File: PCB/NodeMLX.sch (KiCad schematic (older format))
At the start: 19 parts, among them J1 DS3231, J2 PIR, M1 MICROSD, U1 NodeMCUv2, U2 MLX90621

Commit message: Fixed PCB. Added html generators for live map
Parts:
- removed LED1: RED, 1206, symbol LEDSMT1206-RESCUE-NodeMLX
- added D2: RED, LEDs:LED_1206, symbol LED_ALT
- R8: value 130R -> 330R
- S1: footprint TACTILE-SWITCH-SMD -> toolbox:TACTILE-SWITCH-SMD
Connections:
- net 3.3V: now also R7.1; no longer S1.1, S1.2
- net BUTTON: now also R7.2, S1.1, S1.2, U1.D4 (D4/BOOT(h)); no longer R7.1, S1.3, S1.4, U1.D0
- net GND: now also S1.3, S1.4, D2.1 (K); no longer R7.2
- net LED: now also U1.D0; no longer U1.D1
- net PIR: now also U1.D1; no longer U1.D4 (D4/BOOT(h))
- net at R8.2: now also D2.2 (A)
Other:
- moved on the sheet: R7, S1
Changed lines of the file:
@@
 Sheet 1 1
 Title "NodeMLX"
-Date "2017-01-31"
-Rev "1"
+Date "2017-03-13"
+Rev "1.2"
 Comp "Github/Leenix"
 Comment1 ""
@@
 Connection ~ 1200 3500
 Connection ~ 1400 3100
-Text GLabel 2550 1000 2    50   Input ~ 0
+Text GLabel 2550 1400 2    50   Input ~ 0
 BUTTON
 Text GLabel 2550 1200 2    50   BiDi ~ 0
@@
 Text GLabel 3850 1750 0    50   Input ~ 0
 SD_CS
-Text GLabel 2550 1400 2    50   Input ~ 0
+Text GLabel 2550 1100 2    50   Input ~ 0
 PIR
 Text GLabel 2550 1600 2    50   Input ~ 0
@@
 L TAC_SWITCHSMD S1
 U 1 1 58916ADB
-P 4500 4350
-F 0 "S1" H 4400 4600 50  0000 L BNN
-F 1 "TAC_SWITCHSMD" H 4400 4100 50  0001 L BNN
-F 2 "TACTILE-SWITCH-SMD" H 4530 4500 20  0001 C CNN
-F 3 "" H 4500 4350 60  0001 C CNN
-	1    4500 4350
-	0    1    1    0
-$EndComp
-Wire Wire Line
-	4400 4150 4500 4150
-Wire Wire Line
-	4400 4550 4500 4550
+P 4500 4850
+F 0 "S1" H 4400 5100 50  0000 L BNN
+F 1 "TAC_SWITCHSMD" H 4400 4600 50  0001 L BNN
+F 2 "toolbox:TACTILE-SWITCH-SMD" H 4530 5000 20  0001 C CNN
+F 3 "" H 4500 4850 60  0001 C CNN
+	1    4500 4850
+	0    1    1    0
+$EndComp
 $Comp
 L 3.3V #SUPPLY019
@@
 L RESISTOR1206 R7
 U 1 1 589183EC
-P 4500 4850
-F 0 "R7" H 4600 4900 50  0000 L BNN
-F 1 "4K7" H 4350 4720 50  0000 L BNN
-F 2 "Resistors_SMD:R_1206" H 4530 5000 20  0001 C CNN
-F 3 "" H 4500 4850 60  0001 C CNN
-	1    4500 4850
+P 4500 4350
+F 0 "R7" H 4600 4400 50  0000 L BNN
+F 1 "4K7" H 4350 4220 50  0000 L BNN
+F 2 "Resistors_SMD:R_1206" H 4530 4500 20  0001 C CNN
+F 3 "" H 4500 4350 60  0001 C CNN
+	1    4500 4350
 	0    1    1    0
 $EndComp
@@
 P 5800 4200
 F 0 "R8" H 5900 4250 50  0000 L BNN
-F 1 "130R" H 5650 4070 50  0000 L BNN
+F 1 "330R" H 5650 4070 50  0000 L BNN
 F 2 "Resistors_SMD:R_1206" H 5830 4350 20  0001 C CNN
 F 3 "" H 5800 4200 60  0001 C CNN
@@
 Text GLabel 5800 3950 1    50   Input ~ 0
 LED
-Text GLabel 2550 1100 2    50   Output ~ 0
+Text GLabel 2550 1000 2    50   Output ~ 0
 LED
 Wire Wire Line
@@
 Wire Notes Line
 	5550 4950 5550 3700
-$Comp
-L LEDSMT1206-RESCUE-NodeMLX LED1
-U 1 1 5891F8F9
-P 5800 4500
-F 0 "LED1" V 5905 4320 50  0000 L BNN
-F 1 "RED" V 5990 4320 50  0000 L BNN
-F 2 "1206" H 5830 4650 20  0001 C CNN
-F 3 "" H 5800 4500 60  0001 C CNN
-	1    5800 4500
-	1    0    0    -1
+Wire Wire Line
+	4500 4650 4400 4650
+Wire Wire Line
+	4400 5050 4500 5050
+Connection ~ 4500 5050
+Connection ~ 4500 4650
+$Comp
+L LED_ALT D2
+U 1 1 58C652BB
+P 5800 4550
+F 0 "D2" H 5800 4650 50  0000 C CNN
+F 1 "RED" H 5800 4450 50  0000 C CNN
+F 2 "LEDs:LED_1206" H 5800 4550 50  0001 C CNN
+F 3 "" H 5800 4550 50  0000 C CNN
+	1    5800 4550
+	0    -1   -1   0
 $EndComp
 $EndSCHEMATC

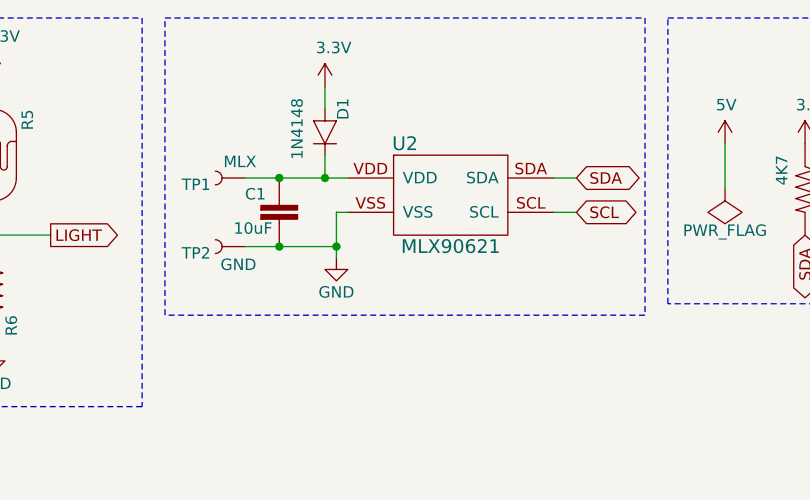
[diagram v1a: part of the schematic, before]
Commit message: Fixed PCB; added callbacks
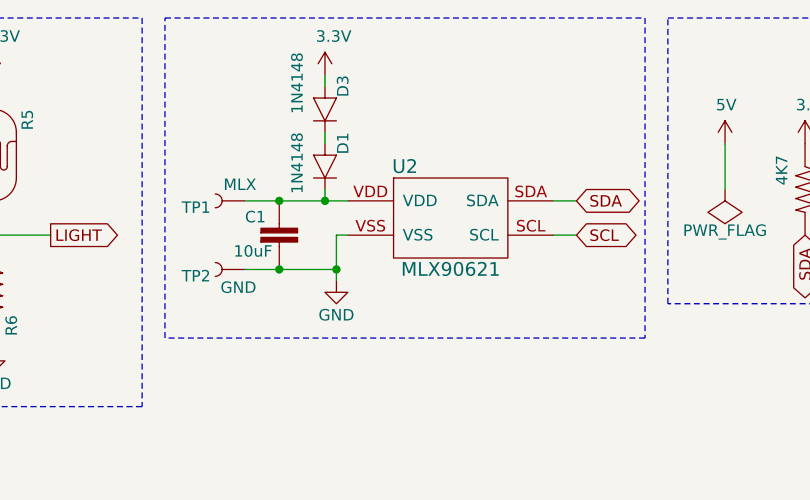
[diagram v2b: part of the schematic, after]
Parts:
- added D3: 1N4148, Diodes_SMD:D_SOD-123, symbol DIODE1N4148
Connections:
- net 3.3V: now also D3.2 (A); no longer D1.2 (A)
- new net: D1.2 (A), D3.1 (C)
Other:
- moved on the sheet: C1, D1, TP1, TP2, U2
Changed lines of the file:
@@
 L MLX90621 U2
 U 1 1 588AF0EC
-P 7850 1350
-F 0 "U2" H 7650 1550 60  0000 C CNN
-F 1 "MLX90621" H 7850 1100 60  0000 C CNN
-F 2 "toolbox:mlx90621" H 7850 1000 60  0001 C CNN
-F 3 "" H 7850 1000 60  0001 C CNN
-	1    7850 1350
+P 7850 1450
+F 0 "U2" H 7650 1650 60  0000 C CNN
+F 1 "MLX90621" H 7850 1200 60  0000 C CNN
+F 2 "toolbox:mlx90621" H 7850 1100 60  0001 C CNN
+F 3 "" H 7850 1100 60  0001 C CNN
+	1    7850 1450
 	1    0    0    -1
 $EndComp
@@
 L DIODE1N4148 D1
 U 1 1 588AF1C1
-P 7300 1100
-F 0 "D1" H 7150 1150 50  0000 L BNN
-F 1 "1N4148" H 7150 950 50  0000 L BNN
-F 2 "Diodes_SMD:D_SOD-123" H 7330 1250 20  0001 C CNN
-F 3 "" H 7300 1100 60  0001 C CNN
-	1    7300 1100
+P 7300 1250
+F 0 "D1" H 7150 1300 50  0000 L BNN
+F 1 "1N4148" H 7150 1100 50  0000 L BNN
+F 2 "Diodes_SMD:D_SOD-123" H 7330 1400 20  0001 C CNN
+F 3 "" H 7300 1250 60  0001 C CNN
+	1    7300 1250
 	0    1    1    0
 $EndComp
@@
 L CAP1206 C1
 U 1 1 588AF2DA
-P 7100 1500
-F 0 "C1" H 6950 1600 50  0000 L BNN
-F 1 "10uF" H 6900 1450 50  0000 L BNN
-F 2 "Capacitors_SMD:C_1206" H 7130 1650 20  0001 C CNN
-F 3 "" H 7100 1500 60  0001 C CNN
-	1    7100 1500
+P 7100 1600
+F 0 "C1" H 6950 1700 50  0000 L BNN
+F 1 "10uF" H 6900 1550 50  0000 L BNN
+F 2 "Capacitors_SMD:C_1206" H 7130 1750 20  0001 C CNN
+F 3 "" H 7100 1600 60  0001 C CNN
+	1    7100 1600
 	1    0    0    -1
 $EndComp
@@
 L GND #PWR01
 U 1 1 588AF3EA
-P 7350 1650
-F 0 "#PWR01" H 7350 1400 50  0001 C CNN
-F 1 "GND" H 7350 1500 50  0000 C CNN
-F 2 "" H 7350 1650 50  0000 C CNN
-F 3 "" H 7350 1650 50  0000 C CNN
-	1    7350 1650
+P 7350 1750
+F 0 "#PWR01" H 7350 1500 50  0001 C CNN
+F 1 "GND" H 7350 1600 50  0000 C CNN
+F 2 "" H 7350 1750 50  0000 C CNN
+F 3 "" H 7350 1750 50  0000 C CNN
+	1    7350 1750
 	1    0    0    -1
 $EndComp
@@
 L TEST-POINT2 TP1
 U 1 1 588B11DC
-P 6950 1300
-F 0 "TP1" H 7100 1300 50  0000 L BNN
-F 1 "MLX" H 6900 1200 50  0000 L BNN
-F 2 "PAD.02X.02" H 6980 1450 20  0001 C CNN
-F 3 "" H 6950 1300 60  0001 C CNN
-	1    6950 1300
+P 6950 1400
+F 0 "TP1" H 7100 1400 50  0000 L BNN
+F 1 "MLX" H 6900 1300 50  0000 L BNN
+F 2 "PAD.02X.02" H 6980 1550 20  0001 C CNN
+F 3 "" H 6950 1400 60  0001 C CNN
+	1    6950 1400
 	-1   0    0    1
 $EndComp
@@
 L TEST-POINT2 TP2
 U 1 1 588B123F
-P 6950 1600
-F 0 "TP2" H 7100 1600 50  0000 L BNN
-F 1 "GND" H 6900 1650 50  0000 L BNN
-F 2 "PAD.02X.02" H 6980 1750 20  0001 C CNN
-F 3 "" H 6950 1600 60  0001 C CNN
-	1    6950 1600
+P 6950 1700
+F 0 "TP2" H 7100 1700 50  0000 L BNN
+F 1 "GND" H 6900 1750 50  0000 L BNN
+F 2 "PAD.02X.02" H 6980 1850 20  0001 C CNN
+F 3 "" H 6950 1700 60  0001 C CNN
+	1    6950 1700
 	-1   0    0    1
 $EndComp
@@
 	2350 1300 2550 1300
 Wire Wire Line
-	7300 1300 7300 1200
-Wire Wire Line
-	7400 1450 7350 1450
-Wire Wire Line
-	7350 1450 7350 1650
-Wire Wire Line
-	6950 1600 7350 1600
-Connection ~ 7350 1600
-Connection ~ 7300 1300
-Wire Wire Line
-	6950 1300 7400 1300
+	7300 1400 7300 1350
+Wire Wire Line
+	7400 1550 7350 1550
+Wire Wire Line
+	7350 1550 7350 1750
+Wire Wire Line
+	6950 1700 7350 1700
+Connection ~ 7350 1700
+Connection ~ 7300 1400
+Wire Wire Line
+	6950 1400 7400 1400
 Wire Wire Line
 	1000 1150 700  1150
@@
 	9700 1150 9700 1150
 Wire Wire Line
-	7300 900  7300 1000
-Wire Wire Line
 	2400 3050 2450 3050
 Wire Wire Line
@@
 Wire Wire Line
 	2400 3250 2450 3250
-Connection ~ 7100 1300
-Connection ~ 7100 1600
-Wire Wire Line
-	8300 1450 8400 1450
+Connection ~ 7100 1400
+Connection ~ 7100 1700
+Wire Wire Line
+	8300 1550 8400 1550
 Wire Wire Line
 	4050 2450 4000 2450
@@
 Text GLabel 2550 2150 2    50   Input ~ 0
 LIGHT
-Text GLabel 8400 1300 2    50   BiDi ~ 0
+Text GLabel 8400 1400 2    50   BiDi ~ 0
 SDA
-Text GLabel 8400 1450 2    50   BiDi ~ 0
+Text GLabel 8400 1550 2    50   BiDi ~ 0
 SCL
 Text GLabel 9400 1550 3    50   BiDi ~ 0
@@
 SCL
 Wire Wire Line
-	8300 1300 8400 1300
+	8300 1400 8400 1400
 Text GLabel 10000 1150 1    50   Input ~ 0
 SD_CS
@@
 	6600 600  8700 600
 Wire Notes Line
-	8700 600  8700 1900
-Wire Notes Line
-	8700 1900 6600 1900
-Wire Notes Line
-	6600 1900 6600 600
+	8700 600  8700 2000
+Wire Notes Line
+	8700 2000 6600 2000
+Wire Notes Line
+	6600 2000 6600 600
 Wire Notes Line
 	1900 2600 2750 2600
@@
 L 3.3V #SUPPLY018
 U 1 1 58915FD9
-P 7300 900
-F 0 "#SUPPLY018" H 7300 900 50  0001 L BNN
-F 1 "3.3V" H 7260 1040 50  0000 L BNN
-F 2 "" H 7300 900 60  0001 C CNN
-F 3 "" H 7300 900 60  0001 C CNN
-	1    7300 900
+P 7300 850
+F 0 "#SUPPLY018" H 7300 850 50  0001 L BNN
+F 1 "3.3V" H 7260 990 50  0000 L BNN
+F 2 "" H 7300 850 60  0001 C CNN
+F 3 "" H 7300 850 60  0001 C CNN
+	1    7300 850
 	1    0    0    -1
 $EndComp
@@
 	0    -1   -1   0
 $EndComp
+$Comp
+L DIODE1N4148 D3
+U 1 1 58DA1B74
+P 7300 1000
+F 0 "D3" H 7150 1050 50  0000 L BNN
+F 1 "1N4148" H 7050 850 50  0000 L BNN
+F 2 "Diodes_SMD:D_SOD-123" H 7330 1150 20  0001 C CNN
+F 3 "" H 7300 1000 60  0001 C CNN
+	1    7300 1000
+	0    1    1    0
+$EndComp
+Wire Wire Line
+	7300 1100 7300 1150
+Wire Wire Line
+	7300 900  7300 850
 $EndSCHEMATC
